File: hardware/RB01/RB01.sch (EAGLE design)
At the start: 10 parts, among them J1 CON_TERMINAL_BLOCK_03-5MM, J2 CON_TERMINAL_BLOCK_02-5MM, K1 JS-M1-12V-5, Q1 BC337

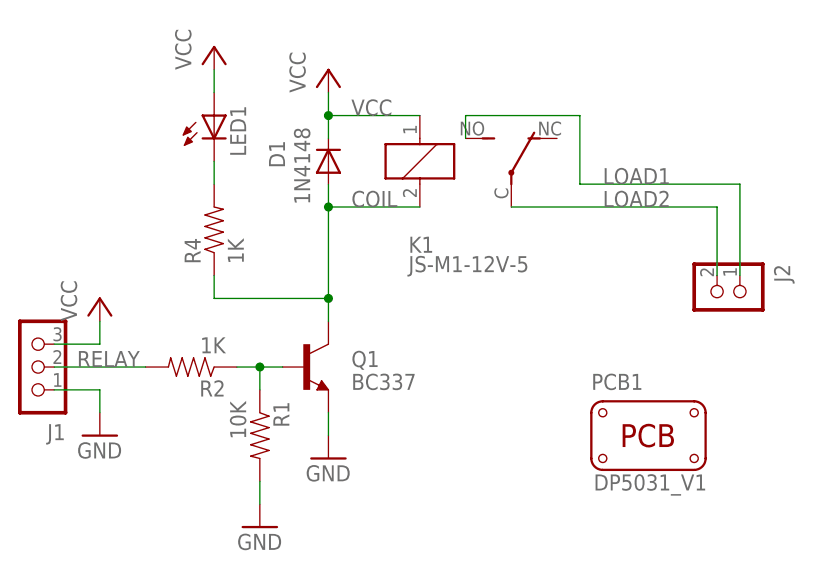
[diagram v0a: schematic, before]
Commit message: hot traces on bottom only
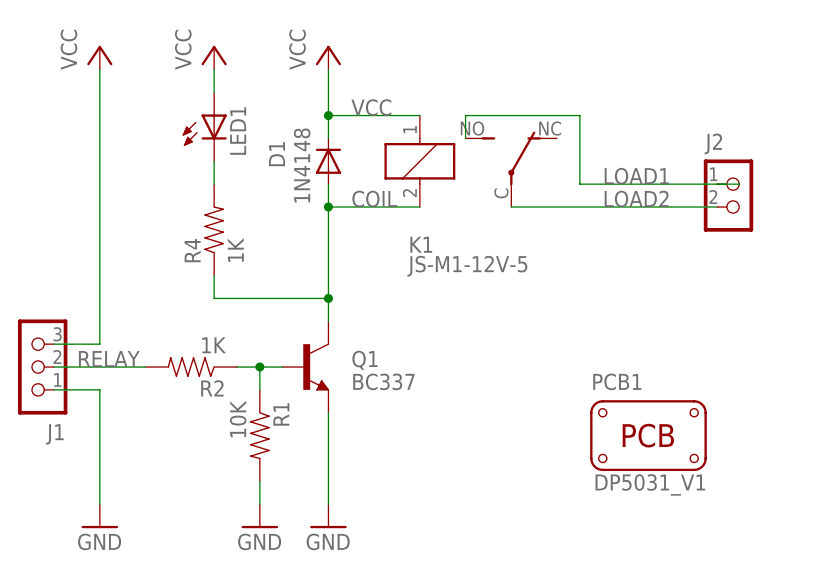
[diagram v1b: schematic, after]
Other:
- moved on the sheet: J2
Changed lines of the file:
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@@
 <instance part="FRAME1" gate="G$1" x="0" y="0"/>
 <instance part="FRAME1" gate="G$2" x="147.32" y="0"/>
-<instance part="GND1" gate="1" x="127" y="76.2"/>
+<instance part="GND1" gate="1" x="127" y="68.58"/>
 <instance part="R2" gate="G$1" x="111.76" y="86.36" rot="R180"/>
 <instance part="LED1" gate="G$1" x="114.3" y="114.3"/>
@@
 </instance>
 <instance part="R1" gate="G$1" x="119.38" y="78.74" rot="R270"/>
-<instance part="GND2" gate="1" x="101.6" y="78.74"/>
+<instance part="GND2" gate="1" x="101.6" y="68.58"/>
 <instance part="GND3" gate="1" x="119.38" y="68.58"/>
 <instance part="J1" gate="CON" x="96.52" y="86.36" rot="R180"/>
-<instance part="J2" gate="CON" x="172.72" y="96.52" rot="R270"/>
+<instance part="J2" gate="CON" x="170.18" y="106.68"/>
 <instance part="Q1" gate="G$1" x="124.46" y="86.36" smashed="yes">
 <attribute name="NAME" x="129.54" y="86.36" size="1.778" layer="95"/>
@@
 <instance part="K1" gate="2" x="147.32" y="106.68" smashed="yes"/>
 <instance part="PCB1" gate="PCB" x="162.56" y="78.74"/>
-<instance part="P+1" gate="VCC" x="101.6" y="93.98"/>
+<instance part="P+1" gate="VCC" x="101.6" y="121.92"/>
 <instance part="P+2" gate="VCC" x="114.3" y="121.92"/>
-<instance part="P+3" gate="VCC" x="127" y="119.38"/>
+<instance part="P+3" gate="VCC" x="127" y="121.92"/>
 </instances>
 <busses>
@@
 <net name="GND" class="0">
 <segment>
-<wire x1="101.6" y1="83.82" x2="101.6" y2="81.28" width="0.1524" layer="91"/>
+<wire x1="101.6" y1="83.82" x2="101.6" y2="71.12" width="0.1524" layer="91"/>
 <pinref part="GND2" gate="1" pin="GND"/>
 <pinref part="J1" gate="CON" pin="1"/>
@@
 <pinref part="GND1" gate="1" pin="GND"/>
 <pinref part="Q1" gate="G$1" pin="E"/>
-<wire x1="127" y1="78.74" x2="127" y2="81.28" width="0.1524" layer="91"/>
+<wire x1="127" y1="71.12" x2="127" y2="81.28" width="0.1524" layer="91"/>
 </segment>
 </net>
@@
 <pinref part="K1" gate="2" pin="P"/>
 <pinref part="J2" gate="CON" pin="2"/>
-<wire x1="170.18" y1="96.52" x2="170.18" y2="104.14" width="0.1524" layer="91"/>
 </segment>
 </net>
 <net name="LOAD1" class="0">
 <segment>
-<wire x1="154.94" y1="106.68" x2="172.72" y2="106.68" width="0.1524" layer="91"/>
+<wire x1="154.94" y1="106.68" x2="170.18" y2="106.68" width="0.1524" layer="91"/>
 <label x="157.48" y="106.68" size="1.778" layer="95"/>
 <pinref part="K1" gate="2" pin="S"/>
@@
 <wire x1="154.94" y1="114.3" x2="154.94" y2="106.68" width="0.1524" layer="91"/>
 <pinref part="J2" gate="CON" pin="1"/>
-<wire x1="172.72" y1="106.68" x2="172.72" y2="96.52" width="0.1524" layer="91"/>
+<wire x1="172.72" y1="106.68" x2="170.18" y2="106.68" width="0.1524" layer="91"/>
 </segment>
 </net>
@@
 <wire x1="96.52" y1="88.9" x2="101.6" y2="88.9" width="0.1524" layer="91"/>
 <pinref part="P+1" gate="VCC" pin="VCC"/>
-<wire x1="101.6" y1="88.9" x2="101.6" y2="91.44" width="0.1524" layer="91"/>
+<wire x1="101.6" y1="88.9" x2="101.6" y2="119.38" width="0.1524" layer="91"/>
 </segment>
 <segment>
@@
 <pinref part="K1" gate="1" pin="1"/>
 <pinref part="P+3" gate="VCC" pin="VCC"/>
-<wire x1="127" y1="114.3" x2="127" y2="116.84" width="0.1524" layer="91"/>
+<wire x1="127" y1="114.3" x2="127" y2="119.38" width="0.1524" layer="91"/>
 <junction x="127" y="114.3"/>
 </segment>

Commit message: faster higher-power diode closer to coil
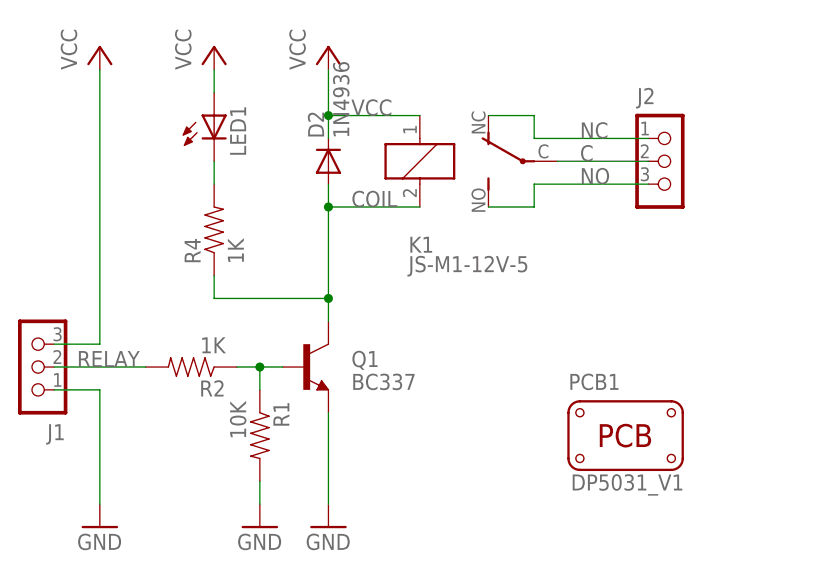
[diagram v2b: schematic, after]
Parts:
- removed D1: 1N4148, SparkFun:DIODE1N4148
- added D2: 1N4936, diode:1N4933
- J2: value CON_TERMINAL_BLOCK_02-5MM -> CON_TERMINAL_BLOCK_03-5MM; device dp_devices:CON_TERMINAL_BLOCK_02-5MM -> dp_devices:CON_TERMINAL_BLOCK_03-5MM
- LED1: device SparkFun:LED5MM -> dp_devices:LED-3MM
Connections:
- net LOAD2 renamed C
- removed net LOAD1: J2.1, K12.S
- new net NC: J2.1, K12.O
- new net NO: J2.3, K12.S
- net COIL: now also D2.A; no longer D1.A
- net VCC: now also D2.C; no longer D1.C
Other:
- moved on the sheet: PCB1
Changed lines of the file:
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@@
 <part name="GND1" library="SparkFun" deviceset="GND" device=""/>
 <part name="R2" library="SparkFun" deviceset="RESISTOR" device="AXIAL-0.3" value="1K"/>
-<part name="LED1" library="SparkFun" deviceset="LED" device="5MM"/>
+<part name="LED1" library="dp_devices" deviceset="LED" device="-3MM"/>
 <part name="R4" library="SparkFun" deviceset="RESISTOR" device="AXIAL-0.3" value="1K"/>
-<part name="D1" library="SparkFun" deviceset="DIODE" device="1N4148" value="1N4148"/>
 <part name="R1" library="SparkFun" deviceset="RESISTOR" device="AXIAL-0.3" value="10K"/>
 <part name="GND2" library="SparkFun" deviceset="GND" device=""/>
 <part name="GND3" library="SparkFun" deviceset="GND" device=""/>
 <part name="J1" library="dp_devices" deviceset="CON_TERMINAL_BLOCK_03" device="-5MM"/>
-<part name="J2" library="dp_devices" deviceset="CON_TERMINAL_BLOCK_02" device="-5MM"/>
+<part name="J2" library="dp_devices" deviceset="CON_TERMINAL_BLOCK_03" device="-5MM"/>
 <part name="Q1" library="transistor" deviceset="BC337" device=""/>
 <part name="K1" library="relay" deviceset="JS-M1*" device="" technology="-12V-5">
@@
 <part name="P+2" library="supply1" deviceset="VCC" device=""/>
 <part name="P+3" library="supply1" deviceset="VCC" device=""/>
+<part name="D2" library="diode" deviceset="1N4933" device="" value="1N4936"/>
 </parts>
 <sheets>
@@
 <instance part="GND1" gate="1" x="127" y="68.58"/>
 <instance part="R2" gate="G$1" x="111.76" y="86.36" rot="R180"/>
-<instance part="LED1" gate="G$1" x="114.3" y="114.3"/>
+<instance part="LED1" gate="LED" x="114.3" y="114.3"/>
 <instance part="R4" gate="G$1" x="114.3" y="101.6" rot="R90"/>
-<instance part="D1" gate="G$1" x="127" y="109.22" smashed="yes" rot="R90">
-<attribute name="NAME" x="122.174" y="108.458" size="1.778" layer="95" rot="R90"/>
-<attribute name="VALUE" x="124.968" y="104.394" size="1.778" layer="96" rot="R90"/>
-</instance>
 <instance part="R1" gate="G$1" x="119.38" y="78.74" rot="R270"/>
 <instance part="GND2" gate="1" x="101.6" y="68.58"/>
 <instance part="GND3" gate="1" x="119.38" y="68.58"/>
 <instance part="J1" gate="CON" x="96.52" y="86.36" rot="R180"/>
-<instance part="J2" gate="CON" x="170.18" y="106.68"/>
+<instance part="J2" gate="CON" x="162.56" y="109.22"/>
 <instance part="Q1" gate="G$1" x="124.46" y="86.36" smashed="yes">
 <attribute name="NAME" x="129.54" y="86.36" size="1.778" layer="95"/>
@@
 <attribute name="PART" x="135.89" y="99.06" size="1.778" layer="95"/>
 </instance>
-<instance part="K1" gate="2" x="147.32" y="106.68" smashed="yes"/>
-<instance part="PCB1" gate="PCB" x="162.56" y="78.74"/>
+<instance part="K1" gate="2" x="149.86" y="109.22" smashed="yes" rot="R90"/>
+<instance part="PCB1" gate="PCB" x="160.02" y="78.74"/>
 <instance part="P+1" gate="VCC" x="101.6" y="121.92"/>
 <instance part="P+2" gate="VCC" x="114.3" y="121.92"/>
 <instance part="P+3" gate="VCC" x="127" y="121.92"/>
+<instance part="D2" gate="1" x="127" y="109.22" rot="R90"/>
 </instances>
 <busses>
@@
 <segment>
 <wire x1="114.3" y1="106.68" x2="114.3" y2="109.22" width="0.1524" layer="91"/>
-<pinref part="LED1" gate="G$1" pin="C"/>
+<pinref part="LED1" gate="LED" pin="C"/>
 <pinref part="R4" gate="G$1" pin="2"/>
 </segment>
@@
 <junction x="127" y="104.14"/>
 <label x="129.54" y="104.14" size="1.778" layer="95"/>
-<pinref part="D1" gate="G$1" pin="A"/>
 <pinref part="R4" gate="G$1" pin="1"/>
 <pinref part="Q1" gate="G$1" pin="C"/>
@@
 <junction x="127" y="93.98"/>
 <pinref part="K1" gate="1" pin="2"/>
-</segment>
-</net>
-<net name="LOAD2" class="0">
-<segment>
-<wire x1="147.32" y1="104.14" x2="170.18" y2="104.14" width="0.1524" layer="91"/>
-<label x="157.48" y="104.14" size="1.778" layer="95"/>
-<pinref part="K1" gate="2" pin="P"/>
-<pinref part="J2" gate="CON" pin="2"/>
-</segment>
-</net>
-<net name="LOAD1" class="0">
-<segment>
-<wire x1="154.94" y1="106.68" x2="170.18" y2="106.68" width="0.1524" layer="91"/>
-<label x="157.48" y="106.68" size="1.778" layer="95"/>
-<pinref part="K1" gate="2" pin="S"/>
-<wire x1="142.24" y1="111.76" x2="142.24" y2="114.3" width="0.1524" layer="91"/>
-<wire x1="142.24" y1="114.3" x2="154.94" y2="114.3" width="0.1524" layer="91"/>
-<wire x1="154.94" y1="114.3" x2="154.94" y2="106.68" width="0.1524" layer="91"/>
-<pinref part="J2" gate="CON" pin="1"/>
-<wire x1="172.72" y1="106.68" x2="170.18" y2="106.68" width="0.1524" layer="91"/>
+<pinref part="D2" gate="1" pin="A"/>
 </segment>
 </net>
@@
 </segment>
 <segment>
-<pinref part="LED1" gate="G$1" pin="A"/>
+<pinref part="LED1" gate="LED" pin="A"/>
 <pinref part="P+2" gate="VCC" pin="VCC"/>
 <wire x1="114.3" y1="116.84" x2="114.3" y2="119.38" width="0.1524" layer="91"/>
@@
 <wire x1="127" y1="114.3" x2="137.16" y2="114.3" width="0.1524" layer="91"/>
 <label x="129.54" y="114.3" size="1.778" layer="95"/>
-<pinref part="D1" gate="G$1" pin="C"/>
 <pinref part="K1" gate="1" pin="1"/>
 <pinref part="P+3" gate="VCC" pin="VCC"/>
 <wire x1="127" y1="114.3" x2="127" y2="119.38" width="0.1524" layer="91"/>
 <junction x="127" y="114.3"/>
+<pinref part="D2" gate="1" pin="C"/>
 </segment>
 </net>
+<net name="C" class="0">
+<segment>
+<pinref part="J2" gate="CON" pin="2"/>
+<pinref part="K1" gate="2" pin="P"/>
+<wire x1="162.56" y1="109.22" x2="152.4" y2="109.22" width="0.1524" layer="91"/>
+<label x="154.94" y="109.22" size="1.778" layer="95"/>
+</segment>
+</net>
+<net name="NC" class="0">
+<segment>
+<pinref part="J2" gate="CON" pin="1"/>
+<wire x1="162.56" y1="111.76" x2="149.86" y2="111.76" width="0.1524" layer="91"/>
+<wire x1="149.86" y1="111.76" x2="149.86" y2="114.3" width="0.1524" layer="91"/>
+<pinref part="K1" gate="2" pin="O"/>
+<wire x1="149.86" y1="114.3" x2="144.78" y2="114.3" width="0.1524" layer="91"/>
+<label x="154.94" y="111.76" size="1.778" layer="95"/>
+</segment>
+</net>
+<net name="NO" class="0">
+<segment>
+<pinref part="J2" gate="CON" pin="3"/>
+<wire x1="162.56" y1="106.68" x2="149.86" y2="106.68" width="0.1524" layer="91"/>
+<wire x1="149.86" y1="106.68" x2="149.86" y2="104.14" width="0.1524" layer="91"/>
+<pinref part="K1" gate="2" pin="S"/>
+<wire x1="149.86" y1="104.14" x2="144.78" y2="104.14" width="0.1524" layer="91"/>
+<label x="154.94" y="106.68" size="1.778" layer="95"/>
+</segment>
+</net>
